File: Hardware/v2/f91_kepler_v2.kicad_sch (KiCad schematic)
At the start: 89 parts, among them J1 LS013B7DH03 FPC, Q1 FS8205A, SW1 BTN1/BSL, SW2 BTN2, SW3 BTN3, U1 CC2652R7RGZ, U2 BQ51050B, U3 DW01A, U4 XC6206P302MR, U5 LIS2DW12, U6 DRV2605L, U7 ST25DV04K, Y1 48MHz FA-128, Y2 32.768kHz FC-135

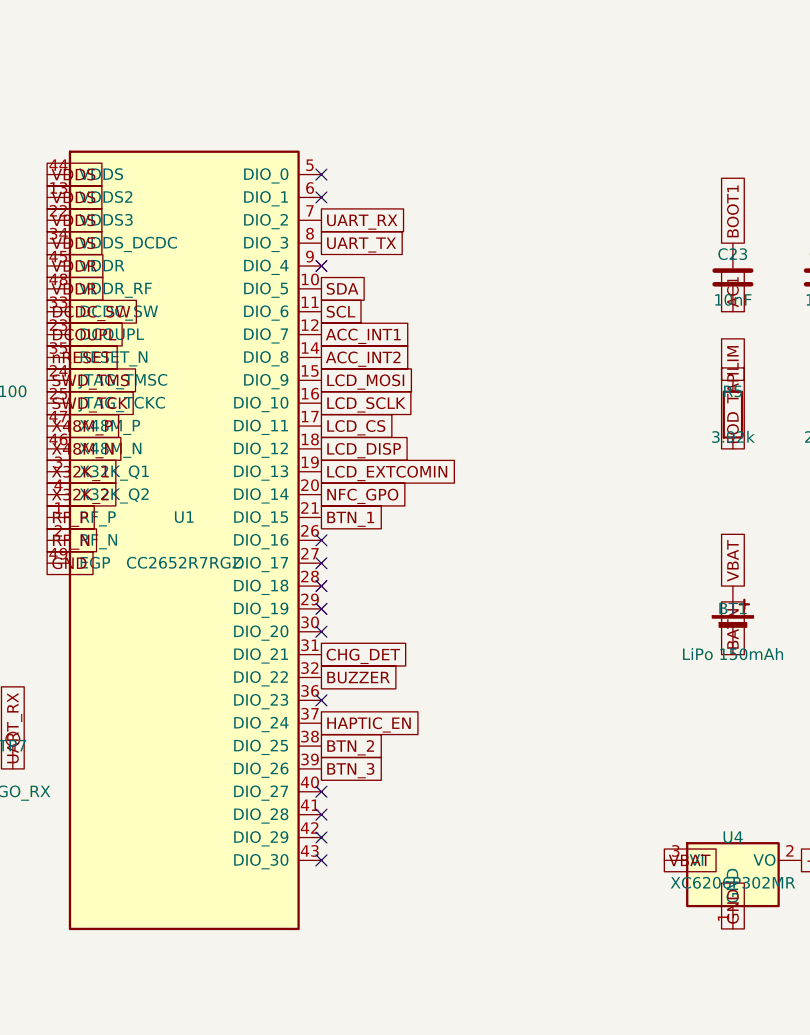
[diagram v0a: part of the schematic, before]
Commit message: feat(hw/v2): pin remap + placement surgery, routing at 54% remaining ratsnest
- re-pin (CC2652 IOC mux): LCD MOSI/SCLK/CS/DISP/EXTCOMIN -> DIO_27-30/26
  (top edge, face J1), BTN_1 -> DIO_0, BTN_3 -> DIO_20, UART_RX/TX ->
  DIO_9/10, ACC_INT2 -> DIO_11; schematic + board + kepler_config.h
  (KEPLER_BOARD_V2 block) + PINMAP.md all in sync, ERC 0
- surgery: U2 +0.7 (U1-U2 channel 0.35 -> 1.05mm), FB1/C22/C23/C26/R7
  cascade south, R3/C11/R5/C18/R4 row north (LCD via lane), U6 west,
  L2/C24 east (U1 right-col lanes), TP15/16 NFC taps into BT1 gap
  beside U7 NFC pins, Y2 north (HAPTIC_EN lane)
- clearance rules 0.2 -> 0.15 (JLC 0.127 capable), edge rule 0.22
- unconnected 198 -> 91; DRC clean except documented corner-arc phantom
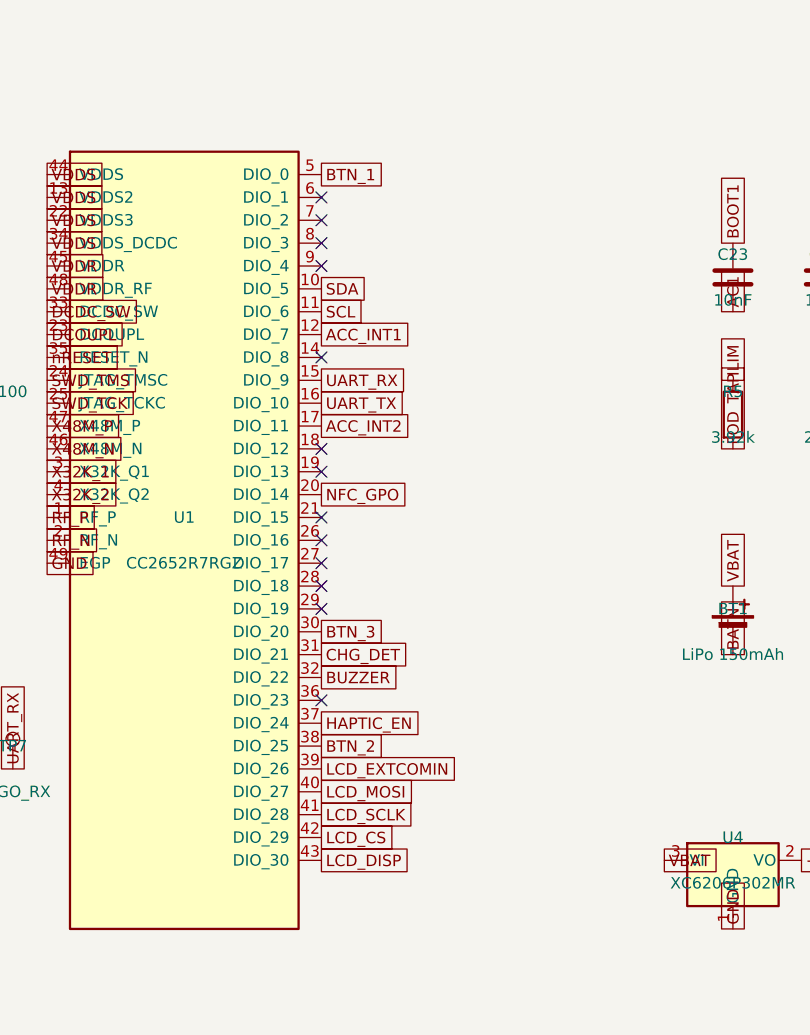
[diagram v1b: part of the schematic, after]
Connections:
- net ACC_INT2: now also U1.17 (DIO_11); no longer U1.14 (DIO_8)
- net BTN_1: now also U1.5 (DIO_0); no longer U1.21 (DIO_15)
- net BTN_3: now also U1.30 (DIO_20); no longer U1.39 (DIO_26)
- net LCD_CS: now also U1.42 (DIO_29); no longer U1.17 (DIO_11)
- net LCD_DISP: now also U1.43 (DIO_30); no longer U1.18 (DIO_12)
- net LCD_EXTCOMIN: now also U1.39 (DIO_26); no longer U1.19 (DIO_13)
- net LCD_MOSI: now also U1.40 (DIO_27); no longer U1.15 (DIO_9)
- net LCD_SCLK: now also U1.41 (DIO_28); no longer U1.16 (DIO_10)
- net UART_RX: now also U1.15 (DIO_9); no longer U1.7 (DIO_2)
- net UART_TX: now also U1.16 (DIO_10); no longer U1.8 (DIO_3)
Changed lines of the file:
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@@
 	(paper "A2")
 	(no_connect
-		(at 134.62 149.86)
+		(at 134.62 86.36)
 	)
 	(no_connect
@@
 	)
 	(no_connect
-		(at 134.62 152.4)
+		(at 134.62 99.06)
 	)
 	(no_connect
@@
 	)
 	(no_connect
-		(at 134.62 78.74)
+		(at 134.62 116.84)
 	)
 	(no_connect
-		(at 134.62 154.94)
+		(at 134.62 109.22)
 	)
 	(no_connect
@@
 	)
 	(no_connect
-		(at 134.62 129.54)
+		(at 134.62 111.76)
 	)
 	(no_connect
@@
 	)
 	(no_connect
-		(at 134.62 147.32)
+		(at 134.62 83.82)
 	)
 	(no_connect
@@
 	(global_label "LCD_EXTCOMIN"
 		(shape passive)
-		(at 134.62 111.76 0)
+		(at 134.62 144.78 0)
 		(effects
 			(font
@@
 		)
 		(property "Intersheetrefs" "${INTERSHEET_REFS}"
-			(at 134.62 111.76 0)
+			(at 134.62 144.78 0)
 			(hide yes)
 			(show_name no)
@@
 	(global_label "UART_TX"
 		(shape passive)
-		(at 134.62 86.36 0)
+		(at 134.62 104.14 0)
 		(effects
 			(font
@@
 		)
 		(property "Intersheetrefs" "${INTERSHEET_REFS}"
-			(at 134.62 86.36 0)
+			(at 134.62 104.14 0)
 			(hide yes)
 			(show_name no)
@@
 	(global_label "UART_RX"
 		(shape passive)
-		(at 134.62 83.82 0)
+		(at 134.62 101.6 0)
 		(effects
 			(font
@@
 		)
 		(property "Intersheetrefs" "${INTERSHEET_REFS}"
-			(at 134.62 83.82 0)
+			(at 134.62 101.6 0)
 			(hide yes)
 			(show_name no)
@@
 	(global_label "ACC_INT2"
 		(shape passive)
-		(at 134.62 99.06 0)
+		(at 134.62 106.68 0)
 		(effects
 			(font
@@
 		)
 		(property "Intersheetrefs" "${INTERSHEET_REFS}"
-			(at 134.62 99.06 0)
+			(at 134.62 106.68 0)
 			(hide yes)
 			(show_name no)
@@
 	(global_label "LCD_SCLK"
 		(shape passive)
-		(at 134.62 104.14 0)
+		(at 134.62 149.86 0)
 		(effects
 			(font
@@
 		)
 		(property "Intersheetrefs" "${INTERSHEET_REFS}"
-			(at 134.62 104.14 0)
+			(at 134.62 149.86 0)
 			(hide yes)
 			(show_name no)
@@
 	(global_label "LCD_CS"
 		(shape passive)
-		(at 134.62 106.68 0)
+		(at 134.62 152.4 0)
 		(effects
 			(font
@@
 		)
 		(property "Intersheetrefs" "${INTERSHEET_REFS}"
-			(at 134.62 106.68 0)
+			(at 134.62 152.4 0)
 			(hide yes)
 			(show_name no)
@@
 	(global_label "LCD_MOSI"
 		(shape passive)
-		(at 134.62 101.6 0)
+		(at 134.62 147.32 0)
 		(effects
 			(font
@@
 		)
 		(property "Intersheetrefs" "${INTERSHEET_REFS}"
-			(at 134.62 101.6 0)
+			(at 134.62 147.32 0)
 			(hide yes)
 			(show_name no)
@@
 	(global_label "LCD_DISP"
 		(shape passive)
-		(at 134.62 109.22 0)
+		(at 134.62 154.94 0)
 		(effects
 			(font
@@
 		)
 		(property "Intersheetrefs" "${INTERSHEET_REFS}"
-			(at 134.62 109.22 0)
+			(at 134.62 154.94 0)
 			(hide yes)
 			(show_name no)
@@
 	(global_label "BTN_1"
 		(shape passive)
-		(at 134.62 116.84 0)
+		(at 134.62 78.74 0)
 		(effects
 			(font
@@
 		)
 		(property "Intersheetrefs" "${INTERSHEET_REFS}"
-			(at 134.62 116.84 0)
+			(at 134.62 78.74 0)
 			(hide yes)
 			(show_name no)
@@
 	(global_label "BTN_3"
 		(shape passive)
-		(at 134.62 144.78 0)
+		(at 134.62 129.54 0)
 		(effects
 			(font
@@
 		)
 		(property "Intersheetrefs" "${INTERSHEET_REFS}"
-			(at 134.62 144.78 0)
+			(at 134.62 129.54 0)
 			(hide yes)
 			(show_name no)

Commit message: wip: snapshot pre-migración
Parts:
- removed U4: XC6206P302MR, Package_TO_SOT_SMD:SOT-23, symbol Regulator_Linear:XC6206PxxxMR
- removed U7: ST25DV04K, Package_SO:SOIC-8_3.9x4.9mm_P1.27mm, symbol RF_NFC:ST25DV04K-IER8C3
- added U4: XC6206P302MR, f91_footprints:Back_SOT-23, symbol f91:XC6206PxxxMR_F91
- added U7: ST25DV04K, f91_footprints:Back_SOIC-8_3.9x4.9mm_P1.27mm, symbol f91:ST25DV04K_SO8
- BT1: footprint f91_footprints:BatteryPads -> f91_footprints:Back_BatteryPads
- C16, C17, C19, C20: footprint Capacitor_SMD:C_0603_1608Metric -> f91_footprints:Back_C_0603_1608Metric
- C18, C21, C22, C23, C24, C25, C26, C27, C28, C29, C30, C31, C32, C33, C36, C37, C38: footprint Capacitor_SMD:C_0402_1005Metric -> f91_footprints:Back_C_0402_1005Metric
- FL1: footprint f91_footprints:Murata_LFB18_1608 -> f91_footprints:F91_Murata_LFB18_1608
- J1: footprint Connector_FFC-FPC:Hirose_FH12-10S-0.5SH_1x10-1MP_P0.50mm_Horizontal -> f91_footprints:F91_LCD_FPC_Hirose_FH12-10
- Q1: footprint Package_SO:TSSOP-8_3x3mm_P0.65mm -> f91_footprints:Back_TSSOP-8_3x3mm_P0.65mm
- R10, R11, R12, R13, R14, R5, R6, R7, R8, W1: footprint Resistor_SMD:R_0402_1005Metric -> f91_footprints:Back_R_0402_1005Metric
- TP1, TP10, TP11, TP12, TP13, TP14, TP15, TP16, TP2, TP3, TP4, TP5, TP6, TP7, TP8, TP9: footprint TestPoint:TestPoint_Pad_1.5x1.5mm -> f91_footprints:Back_TestPoint_Pad_1.5x1.5mm
- U2: footprint f91_footprints:VQFN-20-1EP_4.5x3.5mm_P0.5mm -> f91_footprints:Back_VQFN-20-1EP_4.5x3.5mm_P0.5mm
- U3: footprint Package_TO_SOT_SMD:SOT-23-6 -> f91_footprints:Back_SOT-23-6
- U6: footprint f91_footprints:VSSOP-10_3x3mm_P0.5mm -> f91_footprints:Back_VSSOP-10_3x3mm_P0.5mm
- Y1: footprint f91_footprints:Crystal_SMD_3215-4Pin_3.2x1.5mm -> f91_footprints:Epson_FA-128_2.0x1.6mm
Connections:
- net +3V0: now also U4.2 (VO), U7.8 (VCC)
- net GND: now also U4.1 (VSS), U7.4 (VSS)
- net LCD_CS: now also U1.41 (DIO_28); no longer U1.42 (DIO_29)
- net LCD_EXTCOMIN: now also U1.42 (DIO_29); no longer U1.39 (DIO_26)
- net LCD_SCLK: now also U1.39 (DIO_26); no longer U1.41 (DIO_28)
- net NFC_A: now also U7.2 (AC0)
- net NFC_B: now also U7.3 (AC1)
- net NFC_GPO: now also U7.7 (GPO)
- net SCL: now also U7.6 (SCL)
- net SDA: now also U7.5 (SDA)
- net VBAT: now also U4.3 (VI)
- no-connect marks 18 -> 17
